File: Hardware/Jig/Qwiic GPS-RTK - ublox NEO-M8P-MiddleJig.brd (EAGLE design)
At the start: 95.5 x 94.2 mm, 108 parts, among them J13 U.FL, J3 PTH, U1 NEO-M8P, U2 3.3V

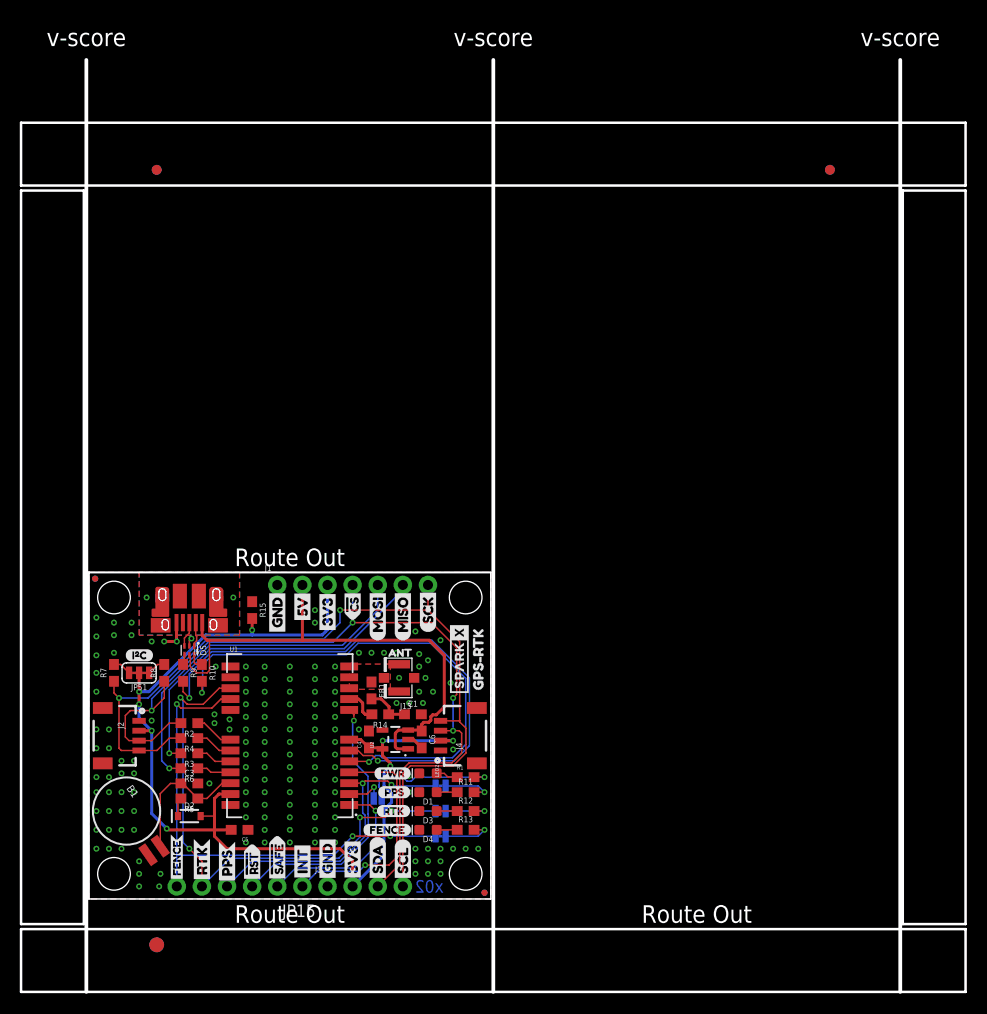
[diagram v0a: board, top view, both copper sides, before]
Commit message: Adding test jig
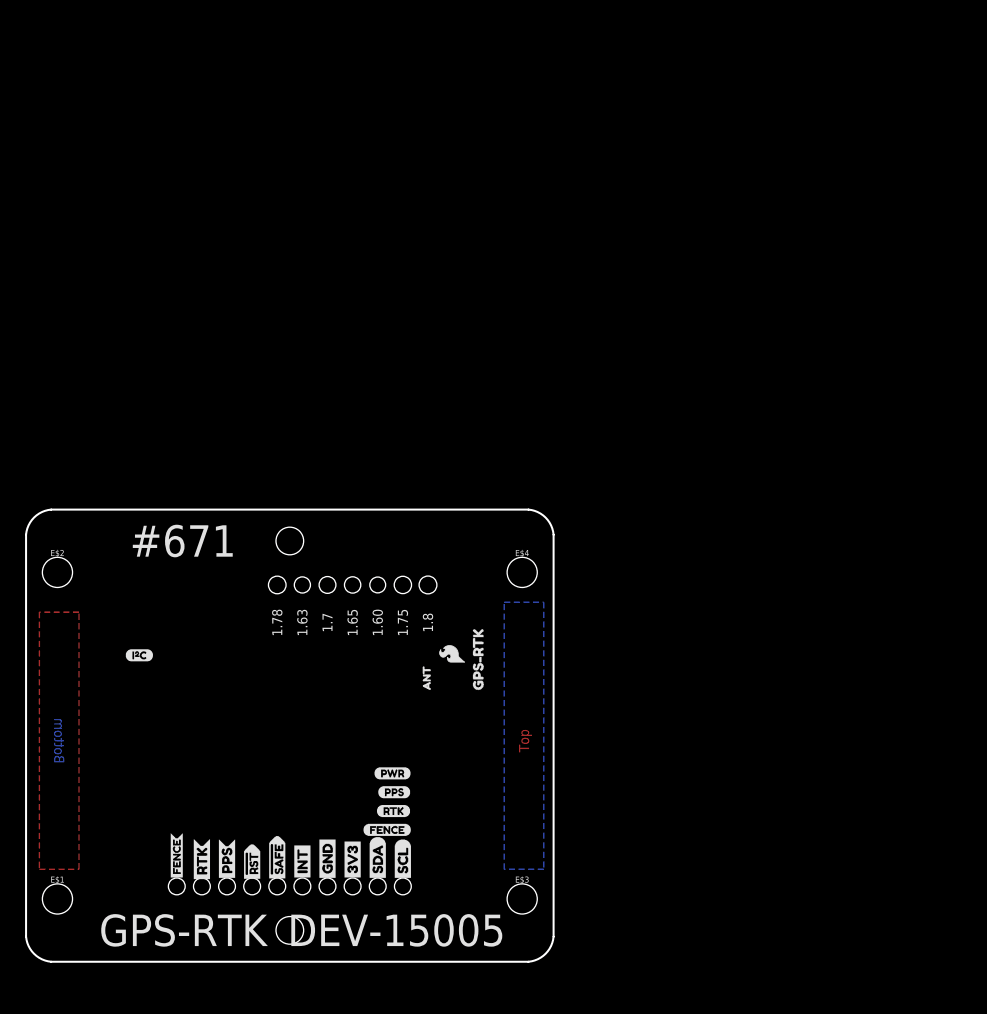
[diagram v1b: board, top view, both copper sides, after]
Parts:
- removed B1: 6.8MM_COIN_CELL, SparkFun-Batteries:BATTCON-6.8MM
- removed C1: 47pF, SparkFun-Capacitors:0603
- removed C3, C4, C6: 1.0uF, SparkFun-Capacitors:0603
- removed C5: 0.1uF, SparkFun-Capacitors:0603
- removed D1, D4: BLUE, SparkFun-LED:LED-0603
- removed D2: 0.5A/40V/420mV, SparkFun-DiscreteSemi:SOD-323
- removed D3: GREEN, SparkFun-LED:LED-0603
- removed D5: PRTR5V0U2F, funbit:SOT886
- removed FB1: 30Ω/1.8A, SparkFun-Coils:0603
- removed J1: (no value), SparkFun-Connectors:1X07_NO_SILK
- removed J13: U.FL, SparkFun-Connectors:U.FL
- removed J2, J4: (no value), SparkFun-Connectors:1X04_1MM_RA
- removed J3: PTH, SparkX:1X04_NO_SILK
- removed J6: (no value), SparkFun-Connectors:USB-MICROB-PTH-MILL
- removed JP1, JP2, JP3: (no value), SparkFun-Jumpers:SMT-JUMPER_2_NC_TRACE_SILK
- removed JP101, JP31, JP41, JP91: STAND-OFF, SparkFun:STAND-OFF
- removed JP15: SPI, SparkFun-Connectors:1X06_NO_SILK
- removed JP21, JP61, JP71, JP81: FIDUCIALUFIDUCIAL, SparkFun:MICRO-FIDUCIAL
- removed JP4: (no value), SparkFun-Jumpers:SMT-JUMPER_2_NO_SILK
- removed JP51: (no value), SparkFun-Jumpers:SMT-JUMPER_3_2-NC_TRACE_SILK
- removed LED2: RED, SparkFun-LED:LED-0603
- removed R1, R11, R12, R13, R5: 1k, SparkFun-Resistors:0603
- removed R10, R9: 27, SparkFun-Resistors:0603
- removed R14: 10, SparkFun-Resistors:0603
- removed R15: 100k, SparkFun-Resistors:0603
- removed R2, R3, R4, R6: 33, SparkFun-Resistors:0603
- removed R7, R8: 2.2k, SparkFun-Resistors:0603
- removed U$19, U$20: (no value), Labels:5V
- removed U$2: SPARKX-LOGO4, SparkX:SPARKX-MEDIUM
- removed U$23, U$24: (no value), Labels:CS#-<]
- removed U$26: (no value), Labels:MISO-(]-04
- removed U$31: SPARKX-LOGO3, SparkX:SPARKX-SMALL
- removed U$34, U$37: (no value), Labels:MOSI-(]-04
- removed U$38, U$41: (no value), Labels:SCK-(]-04
- removed U$60, U$61: (no value), Labels:3V3-04
- removed U$62, U$63: (no value), Labels:GND-04
- removed U1: NEO-M8P, NEO-M8P:NEO-M8P
- removed U2: 3.3V, SparkFun-IC-Power:SOT23-5
- added FRAME1: FRAME-LETTER, SparkFun-Aesthetics:CREATIVE_COMMONS
- added LOGO2: SFE_LOGO_NAME_FLAME.1_INCH, SparkFun-Aesthetics:SFE_LOGO_NAME_FLAME_.1
- E$1, E$2, E$3, E$4: device SparkFun-Aesthetics:FIDUCIAL-1X2 -> SparkFun-Hardware:STAND-OFF-TIGHT
- E$5, E$6: device SparkFun-Retired:FIDUCIAL-1.5X3 -> SparkFun-Hardware:NUBBIN_LOCKER
- U$33: device Labels:MISO-(]-04 -> SparkFun-Aesthetics:SFE_LOGO_FLAME_.1
- moved E$3 80.0 mm to (43.8, 0.00)
- moved E$1 74.4 mm to (-3.17, 0.00)
- moved E$4 51.2 mm to (43.8, 33.0), flipped to the top
- moved E$6 43.0 mm to (20.3, 36.2), flipped to the top
- moved E$2 41.9 mm to (-3.17, 33.0), flipped to the top
- moved E$5 13.5 mm to (20.3, -3.17)
- moved U$33 7.03 mm to (38.4, 23.6), flipped to the top
- moved U$55 6.38 mm to (34.2, 20.4), turned to 90 degrees
- moved U$43 0.25 mm to (14.0, 1.65)
- moved U$44 0.25 mm to (14.0, 1.65)
- moved U$14 0.13 mm to (8.89, 1.78)
- moved U$17 0.13 mm to (8.89, 1.78)
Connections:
- removed net !RESET: JP15.3, U1.8
- removed net !SAFE: JP15.2, U1.1
- removed net 3.3V: C4.1, C5.2, D2.A, J1.3, J2.2, J3.2, J4.2, JP51.2, R1.2, R15.2, U1.23, U1.7, U2.5
- removed net 5V: C6.1, D5.5, J1.2, J6.VBUS, U2.1, U2.3
- removed net ANT_VCC: C1.1, FB1.2, R14.1
- removed net BACKUP: B1.+, C3.1, R5.1, U1.22
- removed net D+: D5.4, R9.1
- removed net D-: D5.6, R10.1
- removed net D_SEL: JP4.2, U1.2
- removed net FENCE_STAT: JP15.6, JP3.2, U1.16
- removed net GND: B1.-, C1.2, C3.2, C4.2, C5.1, C6.2, D1.C, D3.C, D4.C, D5.2, J1.1, J13.1, J13.2, J2.1, J3.1, J4.1, J6.GND, JP4.1, LED2.C, R15.1, U1.10, U1.12, U1.13, U1.24, U2.2
- removed net GPS_ANT1: FB1.1, J13.FEED, U1.11
- removed net INT: JP15.1, U1.4
- removed net N$1: D3.A, R12.1
- removed net N$10: LED2.A, R1.1
- removed net N$11: R9.2, U1.6
- removed net N$12: R10.2, U1.5
- removed net N$13: R14.2, U1.9
- removed net N$2: D1.A, R11.1
- removed net N$3: JP2.1, R12.2
- removed net N$4: JP1.1, R11.2
- removed net N$5: JP51.1, R8.2
- removed net N$6: D2.C, R5.2
- removed net N$7: D4.A, R13.1
- removed net N$8: JP51.3, R7.2
- removed net N$9: JP3.1, R13.2
- removed net PPS: JP1.2, JP15.4, U1.3
- removed net RTK_STAT: JP15.5, JP2.2, U1.15
- removed net RXI/MOSI: J1.5, R6.2
- removed net RXLV: R6.1, U1.21
- removed net SCL/SCK: J1.7, J2.4, J3.4, J4.4, R4.2, R7.1
- removed net SCL_LV: R4.1, U1.19
- removed net SDA/!CS: J1.4, J2.3, J3.3, J4.3, R2.2, R8.1
- removed net SDA_LV: R2.1, U1.18
- removed net SHLD: J6.SHIELD, J6.SHIELD10, J6.SHIELD2, J6.SHIELD3, J6.SHIELD4, J6.SHIELD5, J6.SHIELD6, J6.SHIELD7, J6.SHIELD8, J6.SHIELD9
- removed net TXLV: R3.1, U1.20
- removed net TXO/MISO: J1.6, R3.2
- removed net USB_D+: D5.3, J6.D+
- removed net USB_D-: D5.1, J6.D-
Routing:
- net 3.3V: track 120.0 -> 0.00 mm, vias 9 -> 0
- net SCL/SCK: track 88.7 -> 0.00 mm, vias 2 -> 0
- net SDA/!CS: track 87.4 -> 0.00 mm, vias 4 -> 0
- net N$11: track 55.8 -> 0.00 mm, vias 2 -> 0
- net RTK_STAT: track 53.9 -> 0.00 mm, vias 4 -> 0
- net 5V: track 53.6 -> 0.00 mm
- net N$12: track 52.4 -> 0.00 mm, vias 2 -> 0
- net FENCE_STAT: track 51.4 -> 0.00 mm, vias 3 -> 0
- net RXI/MOSI: track 37.0 -> 0.00 mm, vias 1 -> 0
- net TXO/MISO: track 35.9 -> 0.00 mm, vias 1 -> 0
- net PPS: track 30.6 -> 0.00 mm, vias 2 -> 0
- net !RESET: track 27.6 -> 0.00 mm, vias 1 -> 0
- net INT: track 24.0 -> 0.00 mm, vias 1 -> 0
- net !SAFE: track 18.2 -> 0.00 mm, vias 1 -> 0
- net BACKUP: track 14.1 -> 0.00 mm
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- removed copper zone on layer 16, net GND
- removed copper zone on layer 1, net GPS_ANT1
- removed copper zone on layer 1, net SHLD
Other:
- board size 95.5 x 94.2 mm -> 53.3 x 45.7 mm
- board text added: "#671"
- board text added: "1.60"
- board text added: "1.63"
- board text added: "1.65"
- board text added: "1.7"
- board text added: "1.75"
- board text added: "1.78"
- board text added: "1.8"
- board text added: "Bottom"
- board text added: "DEV-15005"
- board text added: "GPS-RTK"
- board text added: "Measurements in inches"
- board text added: "Top"
- board text removed: "Route Out"
- board text removed: "v-score"
- board text removed: "x02"
